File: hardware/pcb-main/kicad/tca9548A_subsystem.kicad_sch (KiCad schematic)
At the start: 6 parts, among them U4 TCA9548APWR

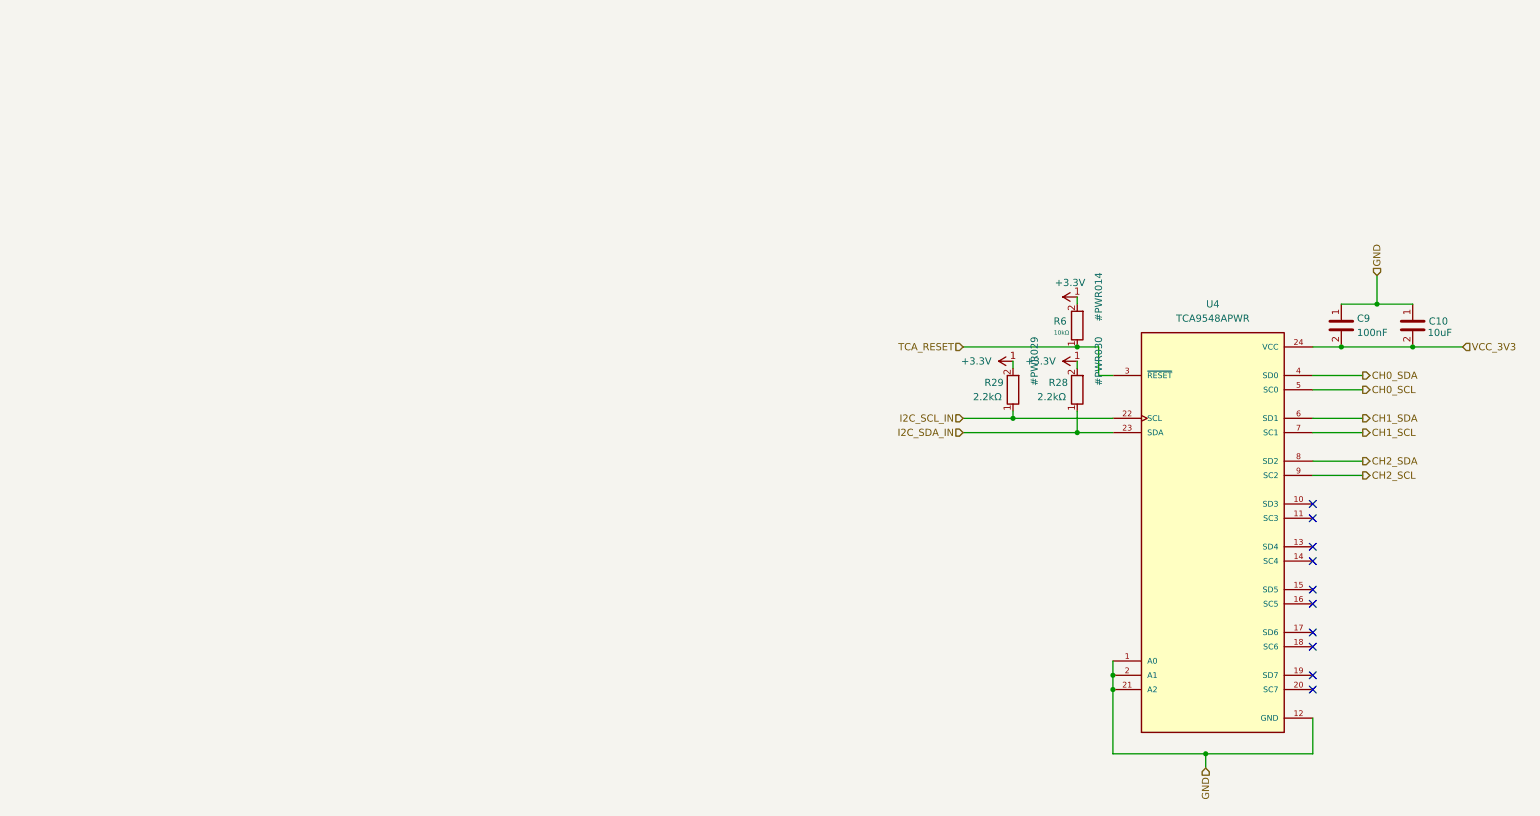
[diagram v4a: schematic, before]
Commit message: Generate ESP32-S3 schematic sheet and apply integration modifications
Phase 1c: created esp32_spec.json and generate_esp32_sheet.py to produce
esp32_s3.kicad_sch with WROOM-1 module, EN/boot circuits, USB series
resistors, decoupling caps, and status LED. All components annotated via
centralized annotate.py.

Phase 1d partial: esp32_integration.py placed AMS1117, USBLC6, power
switch, USB hierarchical labels on power_management sheet; added ESP32
sheet reference and removed U2/U1/unused test points from root sheet.

Fixed modify.py annotate.py path resolution bug. Fixed generator UUID
mismatch that caused kiutils to reset reference designators to '?'.

Made-with: Cursor
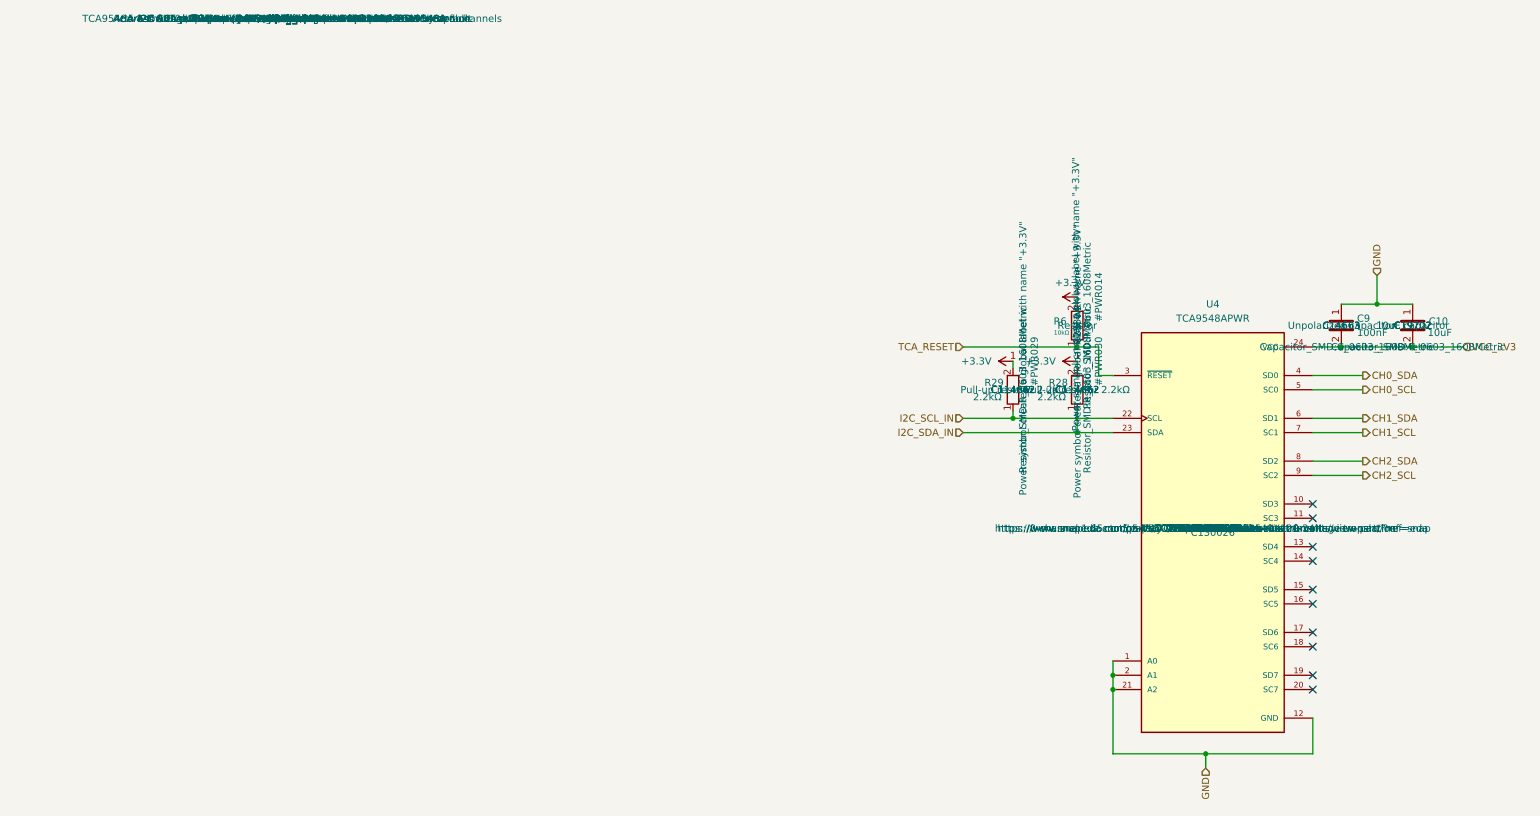
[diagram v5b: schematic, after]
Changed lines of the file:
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@@
 					(size 1.27 1.27)
 				)
-				(hide yes)
 			)
 		)
@@
 					(size 1.27 1.27)
 				)
-				(hide yes)
 			)
 		)
@@
 					(size 1.27 1.27)
 				)
-				(hide yes)
 			)
 		)
@@
 					(size 1.27 1.27)
 				)
-				(hide yes)
 			)
 		)
@@
 					(size 1.27 1.27)
 				)
-				(hide yes)
 			)
 		)
@@
 					(size 1.27 1.27)
 				)
-				(hide yes)
 			)
 		)
@@
 					(size 1.27 1.27)
 				)
-				(hide yes)
 			)
 		)
@@
 					(size 1.27 1.27)
 				)
-				(hide yes)
 			)
 		)
@@
 					(size 1.27 1.27)
 				)
-				(hide yes)
 			)
 		)
@@
 					(size 1.27 1.27)
 				)
-				(hide yes)
 			)
 		)
@@
 					(size 1.27 1.27)
 				)
-				(hide yes)
 			)
 		)
@@
 					(size 1.27 1.27)
 				)
-				(hide yes)
 			)
 		)
@@
 					(size 1.27 1.27)
 				)
-				(hide yes)
 			)
 		)
@@
 					(size 1.27 1.27)
 				)
-				(hide yes)
 			)
 		)
@@
 					(size 1.27 1.27)
 				)
-				(hide yes)
 			)
 		)
@@
 					(size 1.27 1.27)
 				)
-				(hide yes)
 			)
 		)
@@
 					(size 1.27 1.27)
 				)
-				(hide yes)
 			)
 		)
@@
 					(size 1.27 1.27)
 				)
-				(hide yes)
 			)
 		)
@@
 					(size 1.27 1.27)
 				)
-				(hide yes)
 			)
 		)
@@
 					(size 1.27 1.27)
 				)
-				(hide yes)
 			)
 		)
@@
 					(size 1.27 1.27)
 				)
-				(hide yes)
 			)
 		)
@@
 					(size 1.27 1.27)
 				)
-				(hide yes)
 			)
 		)
@@
 					(size 1.27 1.27)
 				)
-				(hide yes)
 			)
 		)
@@
 					(size 1.27 1.27)
 				)
-				(hide yes)
 			)
 		)
@@
 					(size 1.27 1.27)
 				)
-				(hide yes)
 			)
 		)
@@
 					(size 1.27 1.27)
 				)
-				(hide yes)
 			)
 		)
@@
 					(size 1.27 1.27)
 				)
-				(hide yes)
 			)
 		)
@@
 					(size 1.27 1.27)
 				)
-				(hide yes)
 			)
 		)
@@
 					(size 1.27 1.27)
 				)
-				(hide yes)
 			)
 		)
@@
 					(size 1.27 1.27)
 				)
-				(hide yes)
 			)
 		)
@@
 					(size 1.27 1.27)
 				)
-				(hide yes)
 			)
 		)
@@
 					(size 1.27 1.27)
 				)
-				(hide yes)
 			)
 		)
@@
 					(size 1.27 1.27)
 				)
-				(hide yes)
 			)
 		)
@@
 					(size 1.27 1.27)
 				)
-				(hide yes)
 			)
 		)
@@
 					(size 1.27 1.27)
 				)
-				(hide yes)
 			)
 		)
@@
 					(size 1.27 1.27)
 				)
-				(hide yes)
 			)
 		)
@@
 					(size 1.27 1.27)
 				)
-				(hide yes)
 			)
 		)
@@
 					(size 1.27 1.27)
 				)
-				(hide yes)
 			)
 		)
@@
 					(size 1.27 1.27)
 				)
-				(hide yes)
 			)
 		)
@@
 					(size 1.27 1.27)
 				)
-				(hide yes)
 			)
 		)
@@
 					(size 1.27 1.27)
 				)
-				(hide yes)
 			)
 		)
@@
 					(size 1.27 1.27)
 				)
-				(hide yes)
 			)
 		)
@@
 					(size 1.27 1.27)
 				)
-				(hide yes)
 			)
 		)
@@
 					(size 1.27 1.27)
 				)
-				(hide yes)
 			)
 		)
@@
 				)
 				(justify bottom)
-				(hide yes)
 			)
 		)
@@
 					(size 1.27 1.27)
 				)
-				(hide yes)
 			)
 		)
@@
 					(size 1.27 1.27)
 				)
-				(hide yes)
 			)
 		)
@@
 				)
 				(justify bottom)
-				(hide yes)
 			)
 		)
@@
 				)
 				(justify bottom)
-				(hide yes)
 			)
 		)
@@
 				)
 				(justify bottom)
-				(hide yes)
 			)
 		)
@@
 				)
 				(justify bottom)
-				(hide yes)
 			)
 		)
@@
 				)
 				(justify bottom)
-				(hide yes)
 			)
 		)
@@
 				)
 				(justify bottom)
-				(hide yes)
 			)
 		)
@@
 				)
 				(justify bottom)
-				(hide yes)
 			)
 		)
@@
 				)
 				(justify bottom)
-				(hide yes)
 			)
 		)
@@
 				)
 				(justify bottom)
-				(hide yes)
 			)
 		)
@@
 				)
 				(justify bottom)
-				(hide yes)
 			)
 		)
@@
 				)
 				(justify bottom)
-				(hide yes)
 			)
 		)
@@
 				)
 				(justify bottom)
-				(hide yes)
 			)
 		)
@@
 					(size 1.27 1.27)
 				)
-				(hide yes)
 			)
 		)
@@
 				)
 				(justify bottom)
-				(hide yes)
 			)
 		)
@@
 					(size 1.27 1.27)
 				)
-				(hide yes)
 			)
 		)
@@
 					(size 1.27 1.27)
 				)
-				(hide yes)
 			)
 		)
@@
 					(size 1.27 1.27)
 				)
-				(hide yes)
 			)
 		)
@@
 					(size 1.27 1.27)
 				)
-				(hide yes)
 			)
 		)
@@
 					(size 1.27 1.27)
 				)
-				(hide yes)
 			)
 		)
@@
 					(size 1.27 1.27)
 				)
-				(hide yes)
 			)
 		)
@@
 					(size 1.27 1.27)
 				)
-				(hide yes)
 			)
 		)
@@
 					(size 1.27 1.27)
 				)
-				(hide yes)
 			)
 		)
@@
 					(size 1.27 1.27)
 				)
-				(hide yes)
 			)
 		)
@@
 					(size 1.27 1.27)
 				)
-				(hide yes)
 			)
 		)
@@
 					(size 1.27 1.27)
 				)
-				(hide yes)
 			)
 		)
@@
 					(size 1.27 1.27)
 				)
-				(hide yes)
 			)
 		)
@@
 					(size 1.27 1.27)
 				)
-				(hide yes)
-			)
-		)
+			)
+		)

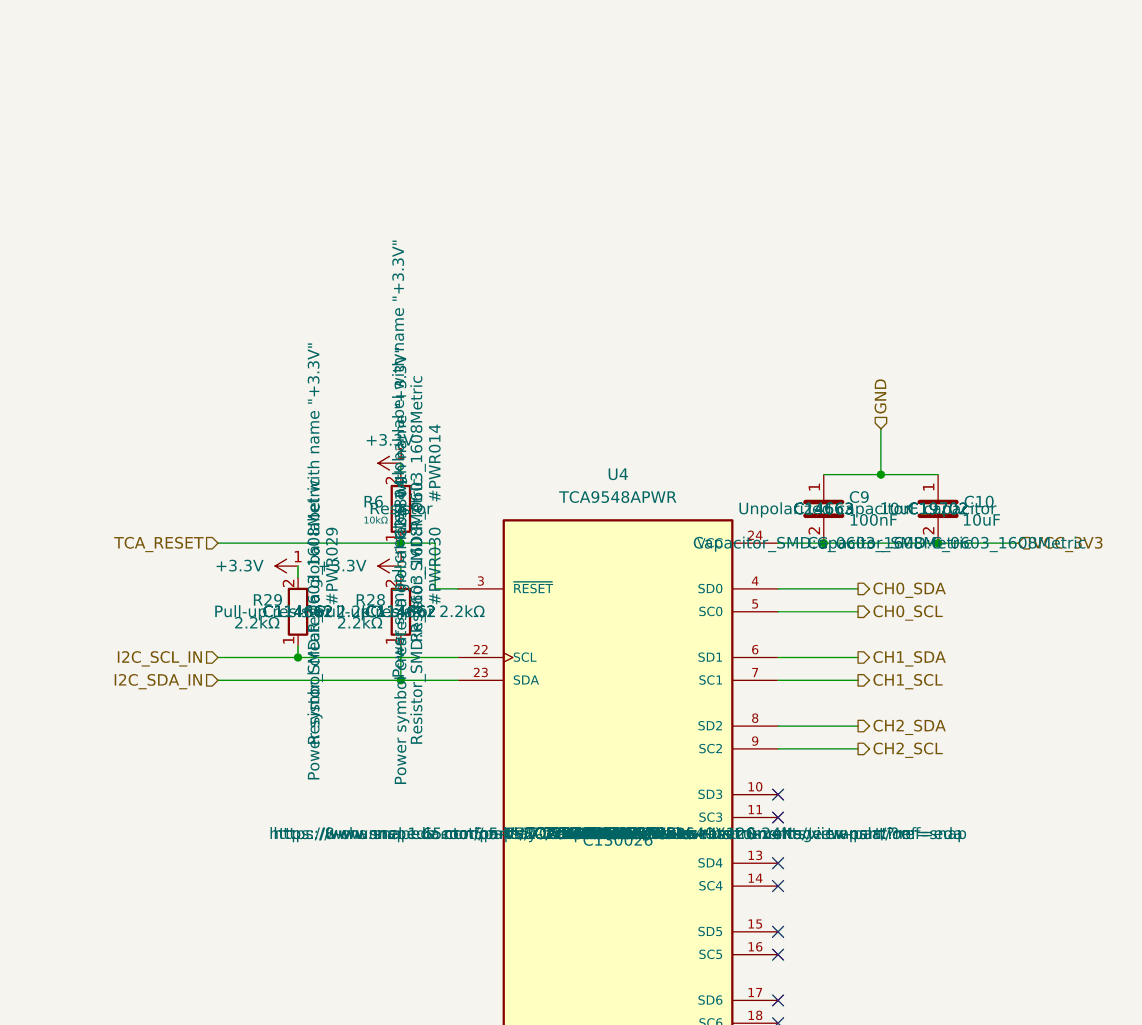
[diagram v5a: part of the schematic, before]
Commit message: Fixed polarity protection on the power circuit
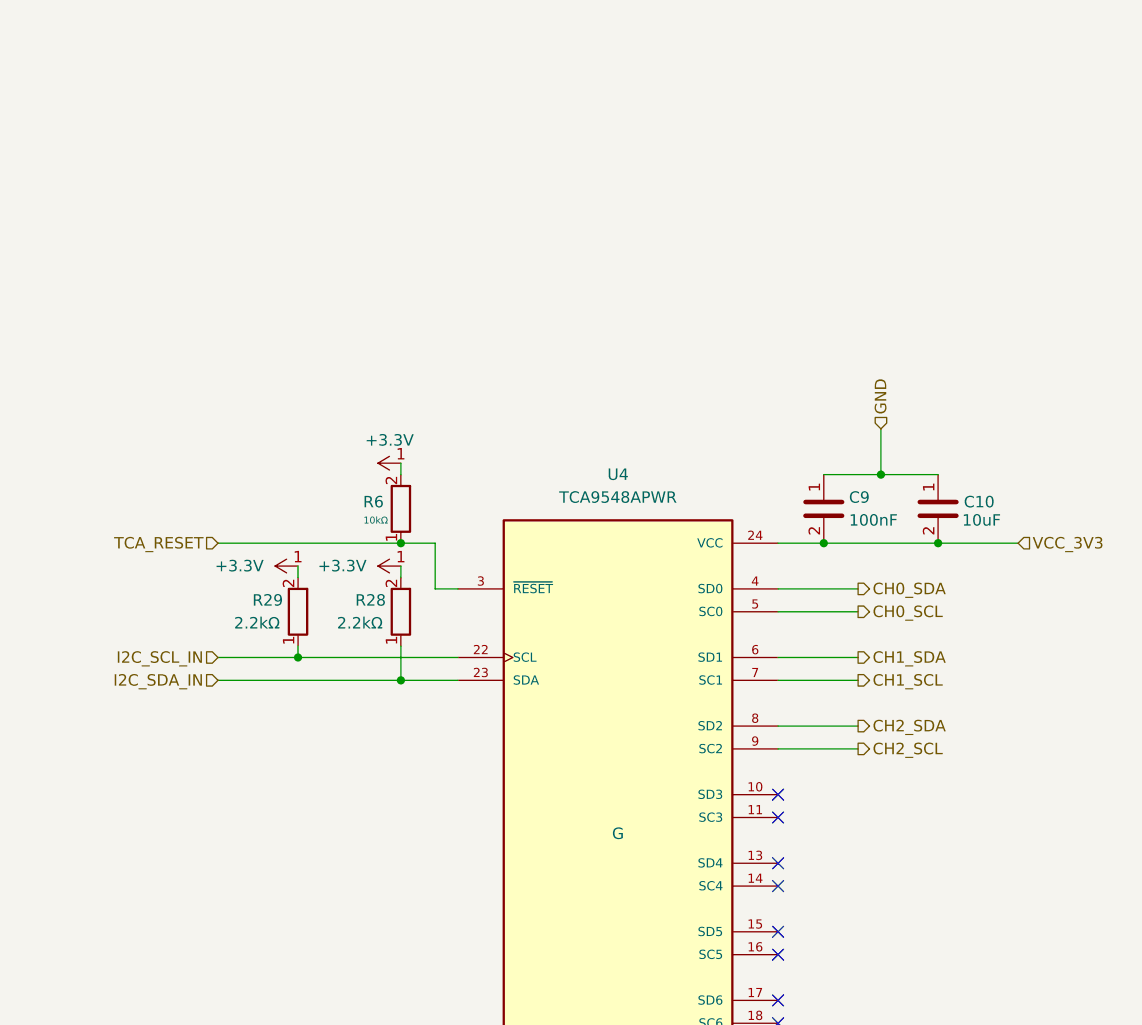
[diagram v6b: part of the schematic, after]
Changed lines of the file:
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@@
 					(size 1.27 1.27)
 				)
+				(hide yes)
 			)
 		)
@@
 					(size 1.27 1.27)
 				)
+				(hide yes)
 			)
 		)
@@
 					(size 1.27 1.27)
 				)
+				(hide yes)
 			)
 		)
@@
 					(size 1.27 1.27)
 				)
+				(hide yes)
 			)
 		)
@@
 					(size 1.27 1.27)
 				)
+				(hide yes)
 			)
 		)
@@
 					(size 1.27 1.27)
 				)
+				(hide yes)
 			)
 		)
@@
 					(size 1.27 1.27)
 				)
+				(hide yes)
 			)
 		)
@@
 					(size 1.27 1.27)
 				)
+				(hide yes)
 			)
 		)
@@
 					(size 1.27 1.27)
 				)
+				(hide yes)
 			)
 		)
@@
 					(size 1.27 1.27)
 				)
+				(hide yes)
 			)
 		)
@@
 					(size 1.27 1.27)
 				)
+				(hide yes)
 			)
 		)
@@
 					(size 1.27 1.27)
 				)
+				(hide yes)
 			)
 		)
@@
 					(size 1.27 1.27)
 				)
+				(hide yes)
 			)
 		)
@@
 					(size 1.27 1.27)
 				)
+				(hide yes)
 			)
 		)
@@
 					(size 1.27 1.27)
 				)
+				(hide yes)
 			)
 		)
@@
 					(size 1.27 1.27)
 				)
+				(hide yes)
 			)
 		)
@@
 					(size 1.27 1.27)
 				)
+				(hide yes)
 			)
 		)
@@
 					(size 1.27 1.27)
 				)
+				(hide yes)
 			)
 		)
@@
 					(size 1.27 1.27)
 				)
+				(hide yes)
 			)
 		)
@@
 					(size 1.27 1.27)
 				)
+				(hide yes)
 			)
 		)
@@
 					(size 1.27 1.27)
 				)
+				(hide yes)
 			)
 		)
@@
 					(size 1.27 1.27)
 				)
+				(hide yes)
 			)
 		)
@@
 					(size 1.27 1.27)
 				)
+				(hide yes)
 			)
 		)
@@
 					(size 1.27 1.27)
 				)
+				(hide yes)
 			)
 		)
@@
 					(size 1.27 1.27)
 				)
+				(hide yes)
 			)
 		)
@@
 				)
 				(justify bottom)
+				(hide yes)
 			)
 		)
@@
 				)
 				(justify bottom)
+				(hide yes)
 			)
 		)
@@
 				)
 				(justify bottom)
+				(hide yes)
 			)
 		)
@@
 				)
 				(justify bottom)
+				(hide yes)
 			)
 		)
@@
 				)
 				(justify bottom)
+				(hide yes)
 			)
 		)
@@
 				)
 				(justify bottom)
+				(hide yes)
 			)
 		)
@@
 				)
 				(justify bottom)
+				(hide yes)
 			)
 		)
@@
 				)
 				(justify bottom)
+				(hide yes)
 			)
 		)
@@
 				)
 				(justify bottom)
+				(hide yes)
 			)
 		)
@@
 				)
 				(justify bottom)
+				(hide yes)
 			)
 		)
@@
 				)
 				(justify bottom)
+				(hide yes)
 			)
 		)
@@
 				)
 				(justify bottom)
+				(hide yes)
 			)
 		)
@@
 					(size 1.27 1.27)
 				)
+				(hide yes)
 			)
 		)
@@
 				)
 				(justify bottom)
+				(hide yes)
 			)
 		)
@@
 					(size 1.27 1.27)
 				)
+				(hide yes)
 			)
 		)
@@
 					(size 1.27 1.27)
 				)
+				(hide yes)
 			)
 		)
@@
 					(size 1.27 1.27)
 				)
+				(hide yes)
 			)
 		)
@@
 					(size 1.27 1.27)
 				)
+				(hide yes)
 			)
 		)
@@
 					(size 1.27 1.27)
 				)
-			)
-		)
+				(hide yes)
+			)
+		)
